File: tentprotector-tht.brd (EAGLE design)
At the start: 40 x 20 mm, 5 parts

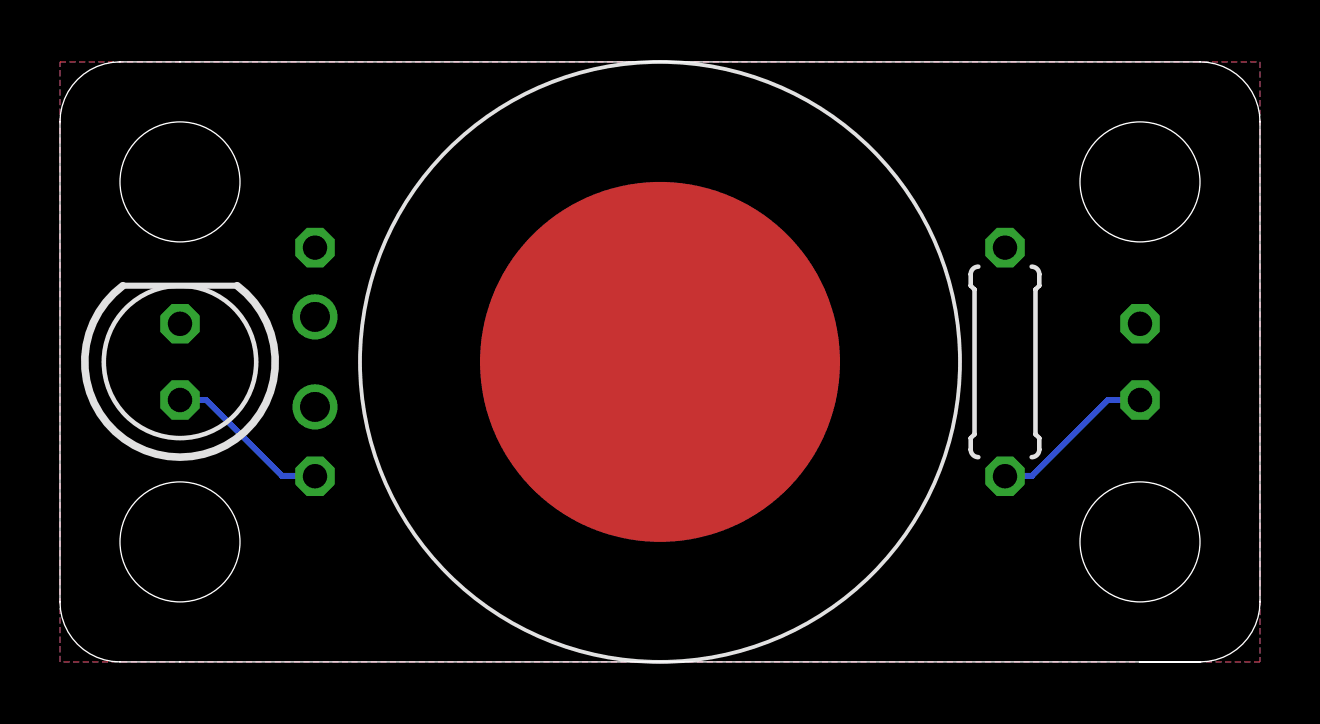
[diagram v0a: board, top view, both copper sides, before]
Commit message: added more variants
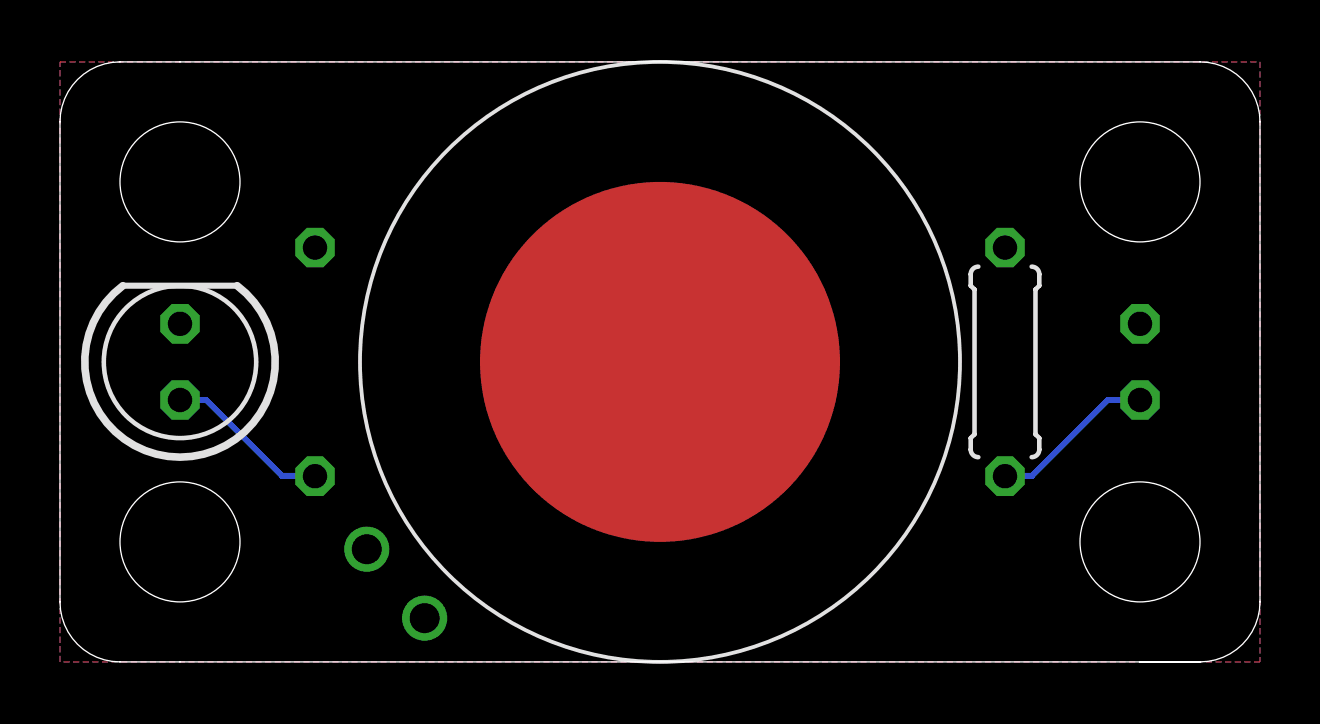
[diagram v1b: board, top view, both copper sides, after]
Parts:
- turned U$1 to 40 degrees
